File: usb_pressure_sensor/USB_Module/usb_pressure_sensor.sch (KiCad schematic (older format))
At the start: 18 parts, among them IC1 STM32F042F6P6, IC2 MCP1700, J2 MODULE_BRIDGE, P1 SWD_TC, SW1 SWITCH_SPST, U1 MICRO_USB, U2 SN74LVC1GX04, Y1 Crystal 32.768kHz

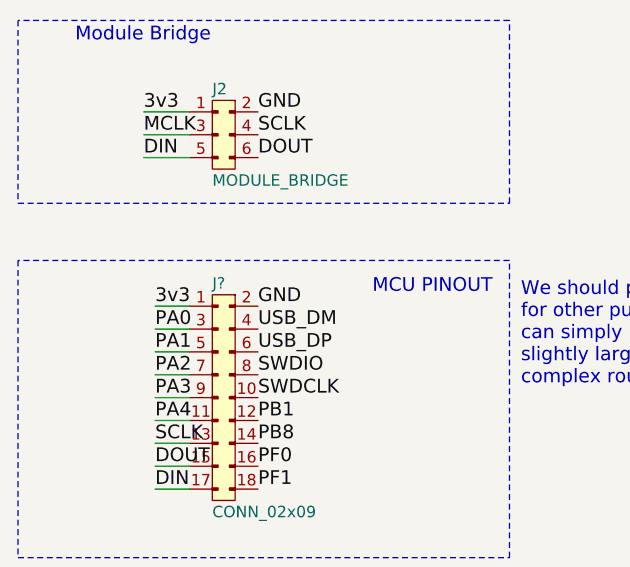
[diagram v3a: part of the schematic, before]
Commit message: PCB design with new pressure sensor and some footprints
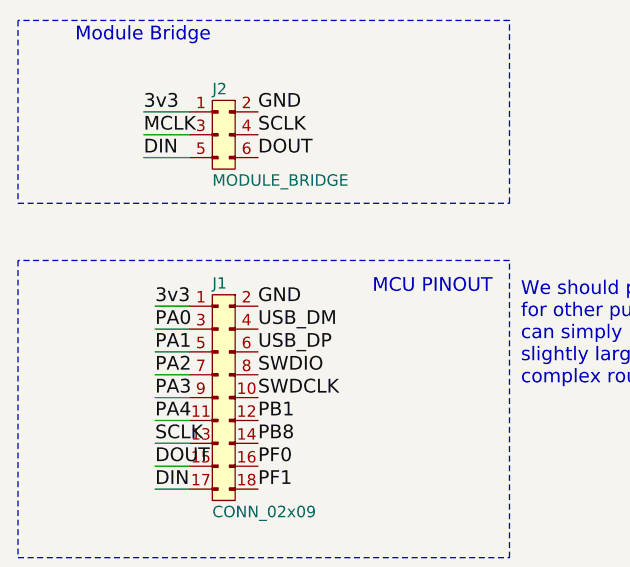
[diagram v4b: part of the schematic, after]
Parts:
- C3, C4: footprint (none) -> Capacitors_SMD:C_0603
- J1: renamed from J?; footprint (none) -> Pin_Headers:Pin_Header_Straight_2x09_Pitch2.54mm
- R3: footprint Resistors_THT:R_Axial_DIN0207_L6.3mm_D2.5mm_P7.62mm_Horizontal -> Resistors_SMD:R_0603
- R4, R5, SW1: footprint (none) -> Resistors_THT:R_Axial_DIN0207_L6.3mm_D2.5mm_P7.62mm_Horizontal
- U2: footprint (none) -> agg:SOT-23-6
- Y1: footprint (none) -> footprints:ABS07-32dot768kHz_Crystal
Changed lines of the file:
@@
 F 0 "SW1" H 7900 2100 50  0000 C CNN
 F 1 "SWITCH_SPST" H 7900 1850 50  0000 C CNN
-F 2 "" H 7900 1950 50  0001 C CNN
+F 2 "Resistors_THT:R_Axial_DIN0207_L6.3mm_D2.5mm_P7.62mm_Horizontal" H 7900 1950 50  0001 C CNN
 F 3 "" H 7900 1950 50  0001 C CNN
 	1    7900 1950
@@
 F 0 "R3" V 8330 2250 50  0000 C CNN
 F 1 "10k" V 8250 2250 50  0000 C CNN
-F 2 "Resistors_THT:R_Axial_DIN0207_L6.3mm_D2.5mm_P7.62mm_Horizontal" V 8180 2250 50  0001 C CNN
+F 2 "Resistors_SMD:R_0603" V 8180 2250 50  0001 C CNN
 F 3 "" H 8250 2250 50  0001 C CNN
 	1    8250 2250
@@
 F 0 "U2" H 8350 4800 60  0000 C CNN
 F 1 "SN74LVC1GX04" H 8650 4400 60  0000 C CNN
-F 2 "" H 8500 4500 60  0001 C CNN
+F 2 "agg:SOT-23-6" H 8500 4500 60  0001 C CNN
 F 3 "" H 8500 4500 60  0001 C CNN
 	1    8500 4600
@@
 F 0 "Y1" H 9750 5300 50  0000 C CNN
 F 1 "Crystal 32.768kHz" H 9750 5000 50  0000 C CNN
-F 2 "" H 9750 5150 50  0001 C CNN
+F 2 "footprints:ABS07-32dot768kHz_Crystal" H 9750 5150 50  0001 C CNN
 F 3 "" H 9750 5150 50  0001 C CNN
 	1    9750 5150
@@
 F 0 "R4" V 9830 4800 50  0000 C CNN
 F 1 "2.2M" V 9750 4800 50  0000 C CNN
-F 2 "" V 9680 4800 50  0001 C CNN
+F 2 "Resistors_THT:R_Axial_DIN0207_L6.3mm_D2.5mm_P7.62mm_Horizontal" V 9680 4800 50  0001 C CNN
 F 3 "" H 9750 4800 50  0001 C CNN
 	1    9750 4800
@@
 F 0 "R5" V 10180 4950 50  0000 C CNN
 F 1 "180k" V 10100 4950 50  0000 C CNN
-F 2 "" V 10030 4950 50  0001 C CNN
+F 2 "Resistors_THT:R_Axial_DIN0207_L6.3mm_D2.5mm_P7.62mm_Horizontal" V 10030 4950 50  0001 C CNN
 F 3 "" H 10100 4950 50  0001 C CNN
 	1    10100 4950
@@
 F 0 "C4" H 10125 5650 50  0000 L CNN
 F 1 "24p" H 10125 5450 50  0000 L CNN
-F 2 "" H 10138 5400 50  0001 C CNN
+F 2 "Capacitors_SMD:C_0603" H 10138 5400 50  0001 C CNN
 F 3 "" H 10100 5550 50  0001 C CNN
 	1    10100 5550
@@
 F 0 "C3" H 9375 5650 50  0000 L CNN
 F 1 "24p" H 9375 5450 50  0000 L CNN
-F 2 "" H 9388 5400 50  0001 C CNN
+F 2 "Capacitors_SMD:C_0603" H 9388 5400 50  0001 C CNN
 F 3 "" H 9350 5550 50  0001 C CNN
 	1    9350 5550
@@
 	3650 6200 1500 6200
 $Comp
-L CONN_02x09 J?
+L CONN_02x09 J1
 U 1 1 599B5AC0
 P 2450 6400
-F 0 "J?" H 2350 6500 50  0000 L CNN
+F 0 "J1" H 2350 6500 50  0000 L CNN
 F 1 "CONN_02x09" H 2350 5500 50  0000 L CNN
-F 2 "" H 2450 6400 50  0001 C CNN
+F 2 "Pin_Headers:Pin_Header_Straight_2x09_Pitch2.54mm" H 2450 6400 50  0001 C CNN
 F 3 "" H 2450 6400 50  0001 C CNN
 	1    2450 6400

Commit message: Routed pin header and swd connector
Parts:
- removed SW1: SWITCH_SPST, Resistors_THT:R_Axial_DIN0207_L6.3mm_D2.5mm_P7.62mm_Horizontal, symbol SWITCH_SPST
- added U3: KSC341J:SWITCH, footprints:KSC431J_SWITCH, symbol KSC341J:SWITCH
- R4, R5: footprint Resistors_THT:R_Axial_DIN0207_L6.3mm_D2.5mm_P7.62mm_Horizontal -> Resistors_SMD:R_0603
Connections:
- wire segments 63 -> 62
- no-connect marks 3 -> 5
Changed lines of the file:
@@
 EESchema Schematic File Version 2
+LIBS:usb_pressure_sensor-rescue
 LIBS:power
 LIBS:device
@@
 GND
 $Comp
-L SWITCH_SPST SW1
-U 1 1 599811CC
-P 7900 1950
-F 0 "SW1" H 7900 2100 50  0000 C CNN
-F 1 "SWITCH_SPST" H 7900 1850 50  0000 C CNN
-F 2 "Resistors_THT:R_Axial_DIN0207_L6.3mm_D2.5mm_P7.62mm_Horizontal" H 7900 1950 50  0001 C CNN
-F 3 "" H 7900 1950 50  0001 C CNN
-	1    7900 1950
-	1    0    0    -1
-$EndComp
-$Comp
 L R R3
 U 1 1 59981239
@@
 Text Label 8250 2550 0    60   ~ 0
 GND
-Text Label 7550 1950 0    60   ~ 0
+Text Label 7300 1850 2    60   ~ 0
 3v3
 $Comp
@@
 	2250 5550 2050 5550
 Wire Wire Line
-	8000 1950 8550 1950
+	7950 1950 8550 1950
 Wire Wire Line
 	8250 1950 8250 2100
@@
 Wire Wire Line
 	8250 2400 8250 2550
-Wire Wire Line
-	7800 1950 7550 1950
 Wire Wire Line
 	3050 1250 3350 1250
@@
 Text Label 2750 2850 0    60   ~ 0
 5v
-$Comp
-L SN74LVC1GX04 U2
-U 1 1 599960D4
-P 8500 4600
-F 0 "U2" H 8350 4800 60  0000 C CNN
-F 1 "SN74LVC1GX04" H 8650 4400 60  0000 C CNN
-F 2 "agg:SOT-23-6" H 8500 4500 60  0001 C CNN
-F 3 "" H 8500 4500 60  0001 C CNN
-	1    8500 4600
-	1    0    0    -1
-$EndComp
 Text Label 8100 4550 0    60   ~ 0
 3v3
@@
 F 0 "R4" V 9830 4800 50  0000 C CNN
 F 1 "2.2M" V 9750 4800 50  0000 C CNN
-F 2 "Resistors_THT:R_Axial_DIN0207_L6.3mm_D2.5mm_P7.62mm_Horizontal" V 9680 4800 50  0001 C CNN
+F 2 "Resistors_SMD:R_0603" V 9680 4800 50  0001 C CNN
 F 3 "" H 9750 4800 50  0001 C CNN
 	1    9750 4800
@@
 F 0 "R5" V 10180 4950 50  0000 C CNN
 F 1 "180k" V 10100 4950 50  0000 C CNN
-F 2 "Resistors_THT:R_Axial_DIN0207_L6.3mm_D2.5mm_P7.62mm_Horizontal" V 10030 4950 50  0001 C CNN
+F 2 "Resistors_SMD:R_0603" V 10030 4950 50  0001 C CNN
 F 3 "" H 10100 4950 50  0001 C CNN
 	1    10100 4950
@@
 MCU
 Wire Notes Line
-	7350 900  7350 2700
-Wire Notes Line
-	7350 2700 10850 2700
+	7100 2700 10850 2700
 Wire Notes Line
 	10850 2700 10850 900
 Wire Notes Line
-	10850 900  7350 900
+	10850 900  7100 900
 Text Notes 3700 3050 0    60   ~ 0
 Chose 22ohm because:\nhttp://www.eevblog.com/forum/projects/why-usb-data-series-resistors/
@@
 Text Notes 3700 6750 0    60   ~ 0
 We should provide a pinout header so that we could reuse this board \nfor other purposes in the future. If these headers are not needed, they\ncan simply be left unsoldered. This will, however, make the board \nslightly larger due to the length of the 2x9 header and the more \ncomplex routes\n
+$Comp
+L SN74LVC1GX04 U2
+U 1 1 59A196E1
+P 8500 4600
+F 0 "U2" H 8350 4800 60  0000 C CNN
+F 1 "SN74LVC1GX04" H 8650 4400 60  0000 C CNN
+F 2 "agg:SOT-23-6" H 8500 4500 60  0001 C CNN
+F 3 "" H 8500 4500 60  0001 C CNN
+	1    8500 4600
+	1    0    0    -1
+$EndComp
+$Comp
+L KSC341J:SWITCH U3
+U 1 1 59A1C27B
+P 7650 1900
+F 0 "U3" H 7550 2050 60  0000 C CNN
+F 1 "KSC341J:SWITCH" H 7850 1750 60  0000 C CNN
+F 2 "footprints:KSC431J_SWITCH" H 7650 1900 60  0001 C CNN
+F 3 "" H 7650 1900 60  0001 C CNN
+	1    7650 1900
+	1    0    0    -1
+$EndComp
+NoConn ~ 7950 1850
+NoConn ~ 7300 1950
+Wire Notes Line
+	7100 900  7100 2700
 $EndSCHEMATC

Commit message: Added LEDs to schematic
Removed cut since the cut needs to be aligned with the usb connector line so the sub connector hangs over the edge of the pcb
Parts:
- added D1, D2: LED, symbol LED
- added R6: R, symbol R
- added R7: 1k, symbol R
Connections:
- wire segments 62 -> 67
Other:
- note added: "For the LED, just copied this http://www.instructables.com/id/Simple-USB-Tester/\nI really don't know how to correctly choose the resistor value since I don't\nknow how much the Data pins can sink so i'll just stick with the instrucbles value of 1k\n"
- note added: "I'm also not sure whether it should go before or after the termination \nresistors\n"
- note added: "LED Design Process:\nPA0 is a TTa pin (from datasheet) which is 3.3V.\nLED is type LGR971 which has forward voltage drop of 2.2V\nLED requires 25mA so resistor value is (1.1)/0.025 = 44 ohms\nNearest lower value we have is 39 ohm 0603"
- note added: "LED type we already have: LGR971 green"

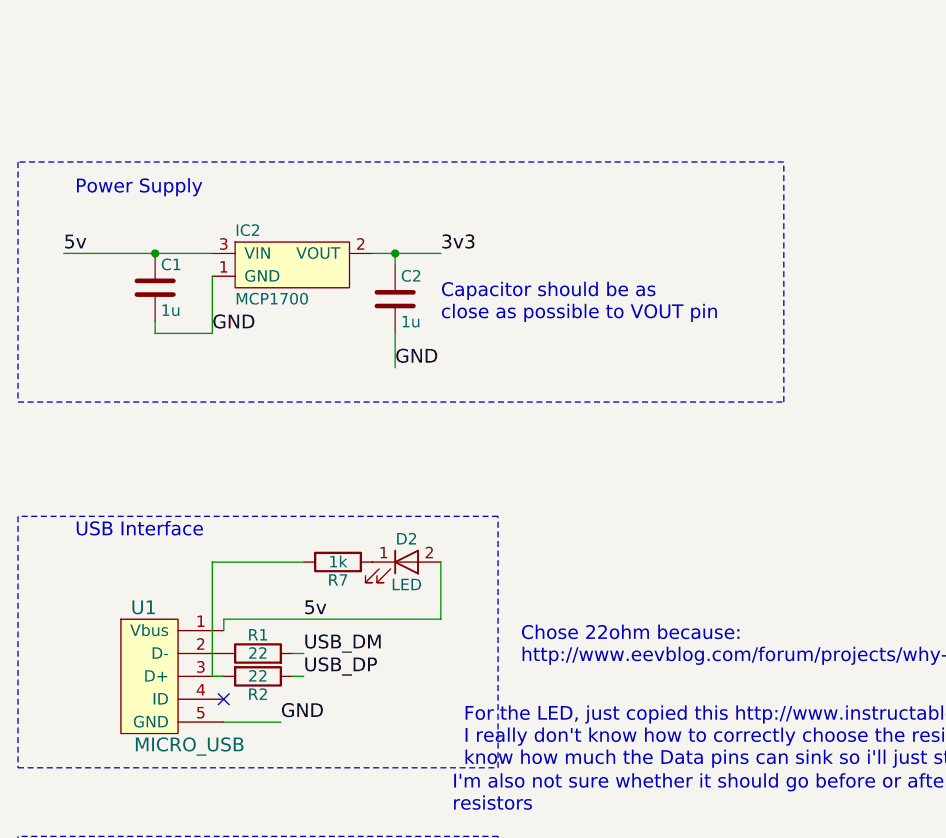
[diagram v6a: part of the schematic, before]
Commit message: added LEDs
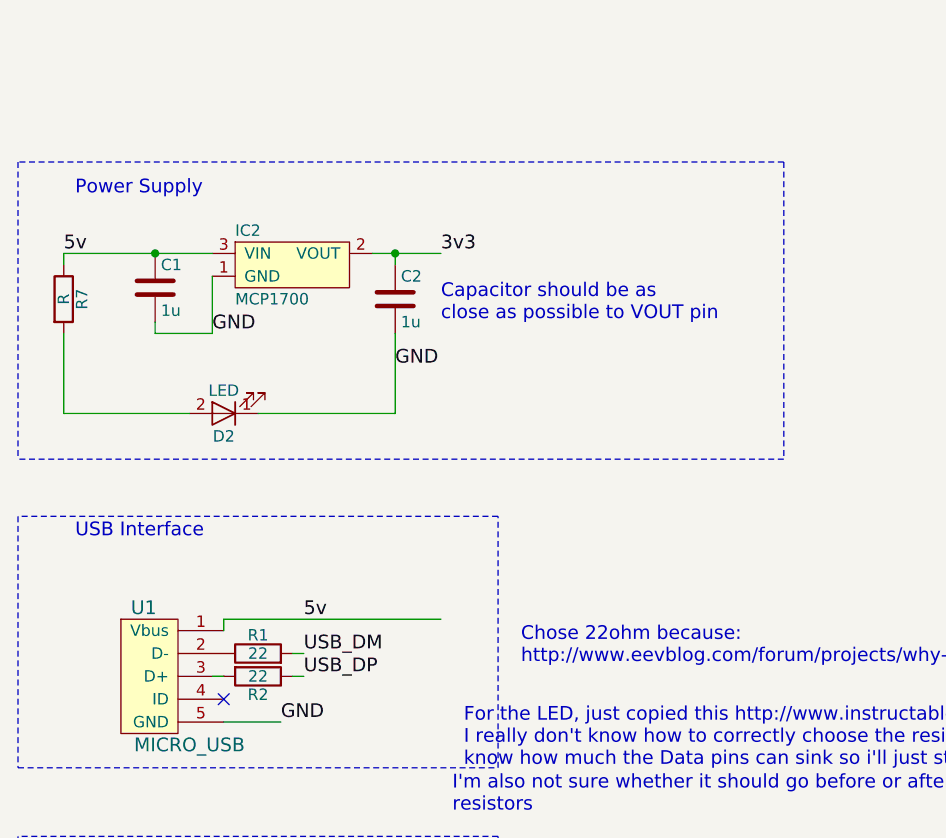
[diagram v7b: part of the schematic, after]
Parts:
- D1, D2: footprint (none) -> LEDs:LED_0805
- R6: footprint (none) -> Resistors_SMD:R_0805
- R7: value 1k -> R; footprint (none) -> Resistors_SMD:R_0805
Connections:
- wire segments 67 -> 68
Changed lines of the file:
@@
 F 0 "D1" H 10400 1350 50  0000 C CNN
 F 1 "LED" H 10400 1150 50  0000 C CNN
-F 2 "" H 10400 1250 50  0001 C CNN
+F 2 "LEDs:LED_0805" H 10400 1250 50  0001 C CNN
 F 3 "" H 10400 1250 50  0001 C CNN
 	1    10400 1250
@@
 F 0 "R6" V 10180 1250 50  0000 C CNN
 F 1 "R" V 10100 1250 50  0000 C CNN
-F 2 "" V 10030 1250 50  0001 C CNN
+F 2 "Resistors_SMD:R_0805" V 10030 1250 50  0001 C CNN
 F 3 "" H 10100 1250 50  0001 C CNN
 	1    10100 1250
@@
 	3150 1250 3150 1300
 Wire Wire Line
-	3150 1600 3150 1750
+	3150 1600 3150 1950
 Wire Wire Line
 	2350 1350 2350 1600
@@
 	2550 5750 2550 5750
 Wire Notes Line
-	1500 850  1500 1900
-Wire Notes Line
-	1500 1900 4850 1900
-Wire Notes Line
-	4850 1900 4850 850
+	1500 850  1500 2150
+Wire Notes Line
+	4850 850  4850 2150
 Wire Notes Line
 	4850 850  1500 850
@@
 Wire Wire Line
 	10550 1250 10650 1250
-$Comp
-L LED D2
-U 1 1 59B46843
-P 3200 2600
-F 0 "D2" H 3200 2700 50  0000 C CNN
-F 1 "LED" H 3200 2500 50  0000 C CNN
-F 2 "" H 3200 2600 50  0001 C CNN
-F 3 "" H 3200 2600 50  0001 C CNN
-	1    3200 2600
-	1    0    0    -1
-$EndComp
-Wire Wire Line
-	2350 2600 2750 2600
 Wire Wire Line
 	2350 3100 2400 3100
 $Comp
 L R R7
-U 1 1 59B470D2
-P 2900 2600
-F 0 "R7" V 2980 2600 50  0000 C CNN
-F 1 "1k" V 2900 2600 50  0000 C CNN
-F 2 "" V 2830 2600 50  0001 C CNN
-F 3 "" H 2900 2600 50  0001 C CNN
-	1    2900 2600
-	0    1    1    0
-$EndComp
-Wire Wire Line
-	3350 2850 3350 2600
-Wire Wire Line
-	2350 2600 2350 3100
+U 1 1 59B782F1
+P 1700 1450
+F 0 "R7" V 1780 1450 50  0000 C CNN
+F 1 "R" V 1700 1450 50  0000 C CNN
+F 2 "Resistors_SMD:R_0805" V 1630 1450 50  0001 C CNN
+F 3 "" H 1700 1450 50  0001 C CNN
+	1    1700 1450
+	1    0    0    -1
+$EndComp
+$Comp
+L LED D2
+U 1 1 59B783A4
+P 2400 1950
+F 0 "D2" H 2400 2050 50  0000 C CNN
+F 1 "LED" H 2400 1850 50  0000 C CNN
+F 2 "LEDs:LED_0805" H 2400 1950 50  0001 C CNN
+F 3 "" H 2400 1950 50  0001 C CNN
+	1    2400 1950
+	-1   0    0    1
+$EndComp
+Wire Wire Line
+	1700 1250 1700 1300
+Wire Wire Line
+	1700 1600 1700 1950
+Wire Wire Line
+	1700 1950 2250 1950
+Wire Wire Line
+	3150 1950 2550 1950
+Wire Notes Line
+	4850 2150 1500 2150
 $EndSCHEMATC

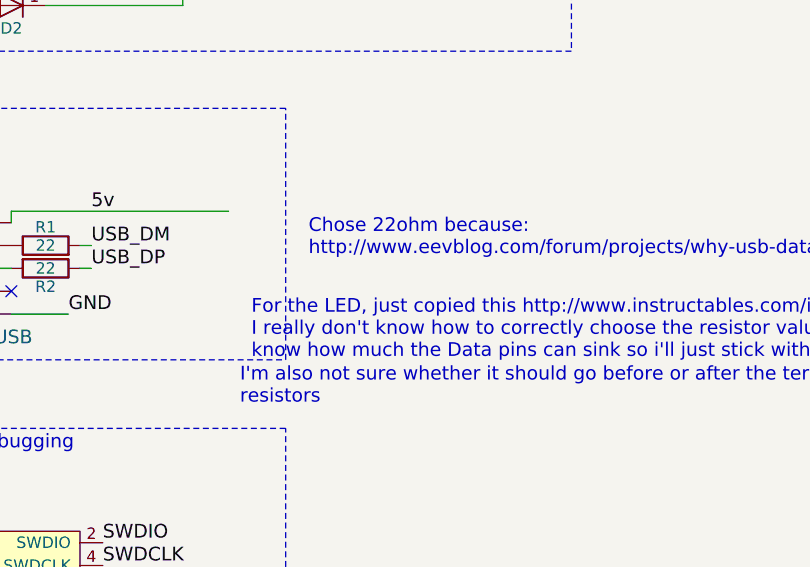
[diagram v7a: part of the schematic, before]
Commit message: Moved usb connector
Moved connector upwards so that the line on the footprint which represents the pcb edge lines up with the actual pcb edge
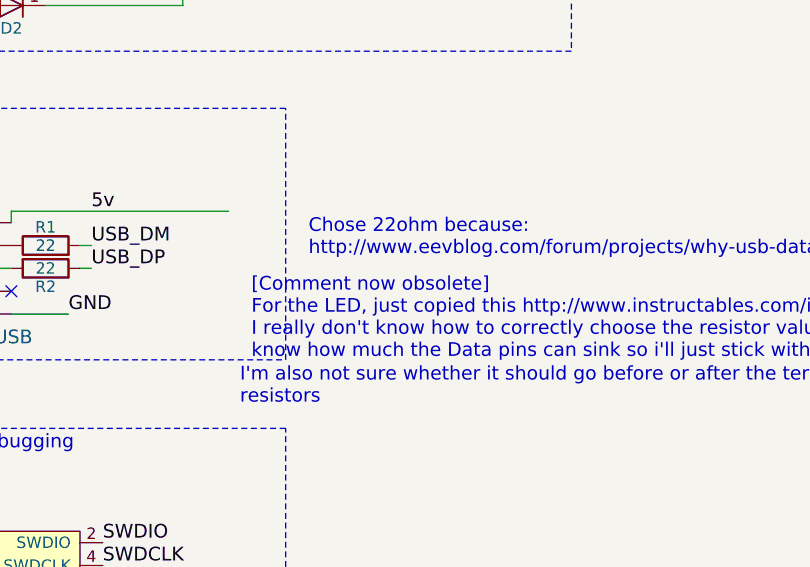
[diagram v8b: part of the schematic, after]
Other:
- note added: "[Comment now obsolete]\nFor the LED, just copied this http://www.instructables.com/id/Simple-USB-Tester/\nI really don't know how to correctly choose the resistor value since I don't\nknow how much the Data pins can sink so i'll just stick with the instrucbles value of 1k\n"
- note removed: "For the LED, just copied this http://www.instructables.com/id/Simple-USB-Tester/\nI really don't know how to correctly choose the resistor value since I don't\nknow how much the Data pins can sink so i'll just stick with the instrucbles value of 1k\n"
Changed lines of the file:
@@
 $EndComp
 Text Notes 3450 3500 0    60   ~ 0
-For the LED, just copied this http://www.instructables.com/id/Simple-USB-Tester/\nI really don't know how to correctly choose the resistor value since I don't\nknow how much the Data pins can sink so i'll just stick with the instrucbles value of 1k\n
+[Comment now obsolete]\nFor the LED, just copied this http://www.instructables.com/id/Simple-USB-Tester/\nI really don't know how to correctly choose the resistor value since I don't\nknow how much the Data pins can sink so i'll just stick with the instrucbles value of 1k\n
 Text Notes 3400 3700 0    60   ~ 0
 I'm also not sure whether it should go before or after the termination \nresistors\n
